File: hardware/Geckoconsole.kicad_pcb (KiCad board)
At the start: 2 copper layers, 68.6 x 41.9 mm, 51 parts, among them J21 I²C, J31 Conn_01x07_Female, J50 USB-C, J71 Conn_01x07, Q51 S8050, Q52 S8050, SW2 Reset, SW41 Rotary_Encoder_Switch, U1 ESP32-WROOM-32, U101 AMS1117-3.3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

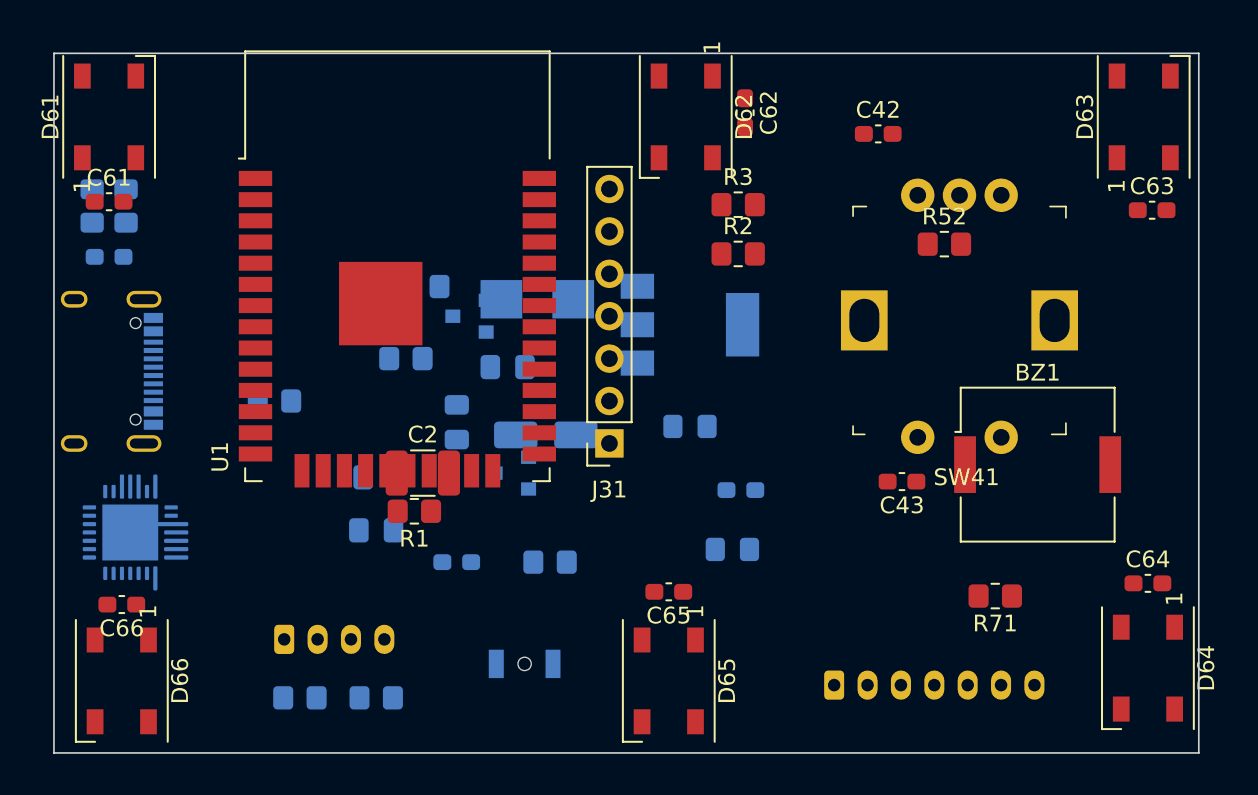
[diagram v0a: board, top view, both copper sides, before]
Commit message: Console Hardware: Place & Route PCB
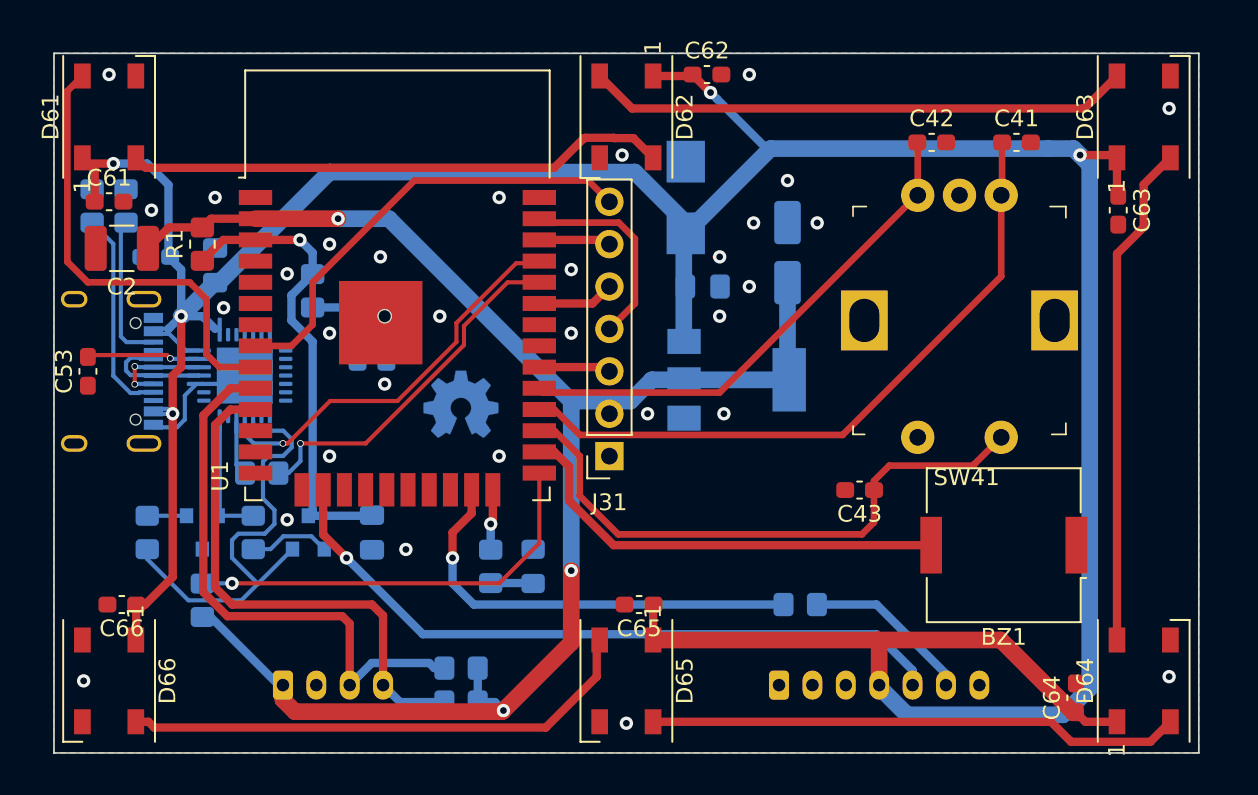
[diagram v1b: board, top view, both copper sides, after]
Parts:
- removed D102: LED, LED_SMD:LED_0805_2012Metric_Pad1.15x1.40mm_HandSolder
- removed R2: 470R, Resistor_SMD:R_0805_2012Metric_Pad1.20x1.40mm_HandSolder
- added LOGO1: Logo_Open_Hardware_Small, Fraxinas:OSHW-Logo_5.7x6mm_Mask, B.Cu at (75.2, 57.7)
- C41: moved to F.Cu
- C53: footprint Capacitor_SMD:C_0805_2012Metric_Pad1.18x1.45mm_HandSolder -> Capacitor_SMD:C_0603_1608Metric_Pad1.08x0.95mm_HandSolder; moved to F.Cu
- R3, R52, R71: moved to B.Cu
- moved R52 44.9 mm to (62.7, 64.3), turned to 90 degrees
- moved C41 26.6 mm to (108.5, 40.9)
- moved R3 26.3 mm to (77.0, 66.3), turned to 90 degrees
- moved R53 23.0 mm to (59.7, 68.3), turned to 90 degrees
- moved C2 22.5 mm to (54.9, 47.2), turned to 180 degrees
- moved SW2 22.5 mm to (70.6, 51.3)
- moved R55 21.6 mm to (66.3, 49.8), turned to 90 degrees
- moved Q51 20.6 mm to (59.7, 64.3), turned to 270 degrees
- moved R1 20.4 mm to (59.7, 47.0), turned to 90 degrees
- moved R51 18.7 mm to (56.4, 64.3), turned to 270 degrees
- moved C53 18.6 mm to (52.8, 54.6), turned to 90 degrees
- moved C102 18.1 mm to (94.7, 47.5), turned to 90 degrees
- moved C51 17.3 mm to (60.5, 48.3), turned to 90 degrees
- moved C55 13.0 mm to (69.8, 54.1), turned to 0 degrees
- moved Q52 12.7 mm to (66.0, 64.3), turned to 90 degrees
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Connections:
- BZ1 pad 1: Net-(BZ1-Pad1) -> GND
- BZ1 pad 2: GND -> Net-(BZ1-Pad2)
- J31 pad 4: SPI_MISO -> SPI_MOSI
- U1 pad 13: TX1 -> (no net)
- U1 pad 14: ENC_SW -> (no net)
- U1 pad 16: RGB -> TX1
- U1 pad 26: ENC_A -> Net-(BZ1-Pad2)
- U1 pad 27: SPI_BL -> ENC_SW
- U1 pad 28: SPI_DC -> ENC_A
- U1 pad 31: SPI_MISO -> (no net)
- U1 pad 36: (no net) -> SPI_DC
- U1 pad 37: (no net) -> SPI_MOSI
- U1 pad 8: Net-(BZ1-Pad1) -> SPI_BL
- U1 pad 9: (no net) -> RGB
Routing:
- net +5V: track 0.00 -> 210.8 mm, vias 0 -> 5
- net +3V3: track 0.00 -> 95.0 mm, vias 0 -> 3
- net TX1: track 0.00 -> 42.2 mm, vias 0 -> 1
- net ENC_A: track 0.00 -> 40.3 mm
- net ENC_SW: track 0.00 -> 35.7 mm
- net I2C_SDI: track 0.00 -> 34.0 mm
- net Net-(D62-Pad2): track 0.00 -> 32.6 mm
- net Net-(D61-Pad2): track 0.00 -> 32.5 mm
- net Net-(D64-Pad2): track 0.00 -> 32.0 mm
- net I2C_SCK: track 0.00 -> 31.6 mm
- net Net-(D65-Pad2): track 0.00 -> 31.3 mm
- net ENC_B: track 0.00 -> 30.9 mm
- net Net-(D63-Pad2): track 0.00 -> 30.2 mm
- net EN: track 0.00 -> 28.2 mm, vias 0 -> 1
- net IO0: track 0.00 -> 27.5 mm, vias 0 -> 1
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- added copper zone on B.Cu, net GND
- added copper zone on F.Cu, net GND

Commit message: Console Hardware: Add Extension header, PCB silkscreen labels
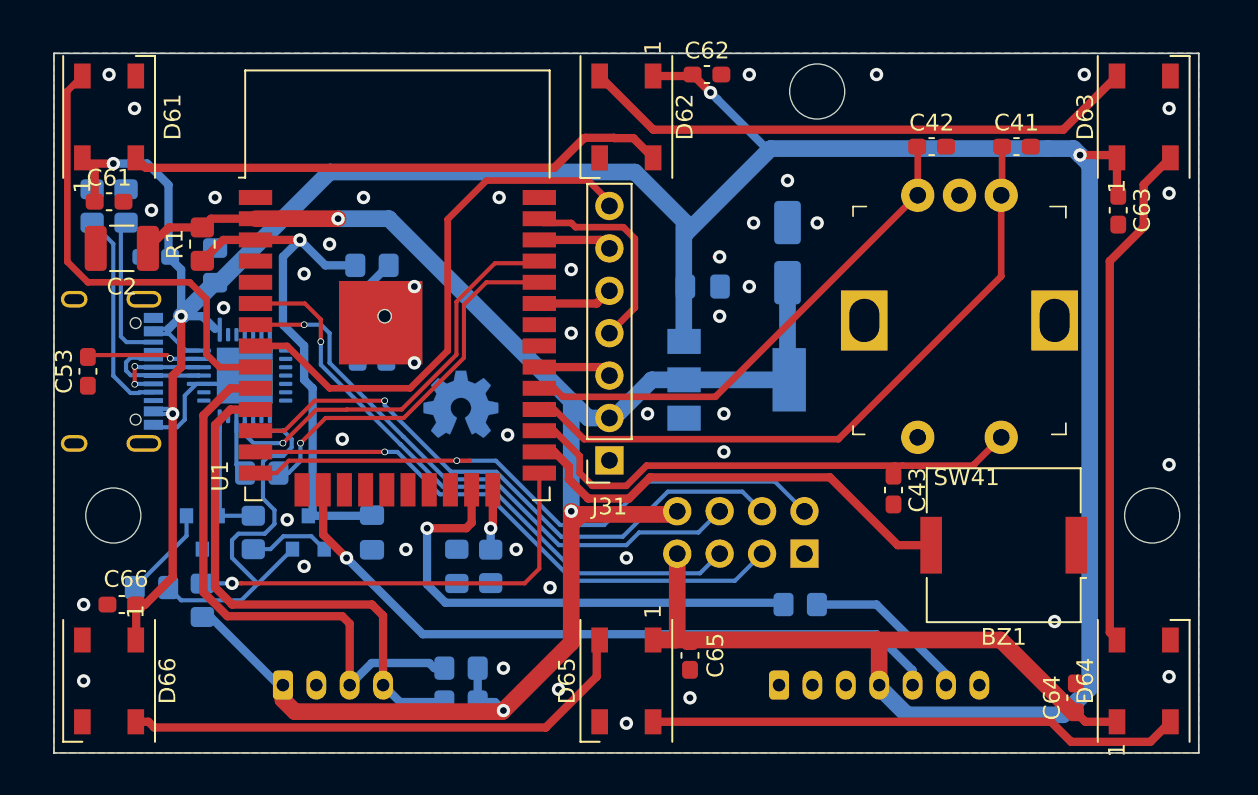
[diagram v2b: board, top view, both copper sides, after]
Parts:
- removed D101: B240, Diode_SMD:D_SMB
- added J1: Conn_01x08_Male, Connector_PinHeader_2.54mm:PinHeader_2x04_P2.54mm_Vertical, B.Cu at (95.8, 65.5)
- moved D1 4.57 mm to (74.9, 66.3)
- moved C65 4.31 mm to (88.9, 71.6), turned to 270 degrees
- moved R55 3.87 mm to (69.8, 48.3), turned to 180 degrees
- moved R51 3.31 mm to (56.6, 67.6), turned to 0 degrees
- moved C43 2.03 mm to (101.1, 61.7), turned to 270 degrees
- moved C41 0.25 mm to (108.5, 41.1)
- moved C42 0.25 mm to (103.4, 41.1)
- moved J31 0.25 mm to (84.1, 59.9)
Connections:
- U1 pad 12: (no net) -> GPIO27
- U1 pad 13: (no net) -> GPIO14
- U1 pad 14: (no net) -> GPIO12
- U1 pad 6: (no net) -> GPIO34
- U1 pad 7: (no net) -> GPIO35
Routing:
- net GPIO12: track 0.00 -> 37.4 mm, vias 0 -> 1
- net GPIO34: track 0.00 -> 36.6 mm, vias 0 -> 1
- net GPIO27: track 0.00 -> 36.2 mm, vias 0 -> 1
- net GPIO35: track 0.00 -> 35.2 mm, vias 0 -> 1
- net GPIO14: track 0.00 -> 34.2 mm, vias 0 -> 1
- net +3V3: track 95.0 -> 102.6 mm
- net SPI_BL: track 27.3 -> 32.5 mm
- net ENC_SW: track 35.7 -> 31.6 mm
- net EN: track 28.2 -> 32.1 mm
- net RX1: track 26.5 -> 30.0 mm
- net +5V: track 210.8 -> 214.1 mm
- net Net-(Q51-Pad1): track 2.35 -> 5.59 mm
- net /RTS: track 27.4 -> 24.9 mm
- net Net-(D1-Pad2): track 2.55 -> 0.00 mm
- net RXD0: track 21.7 -> 22.9 mm
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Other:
- outline, holes or cut-outs redrawn

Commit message: Console PCB: Drill holes
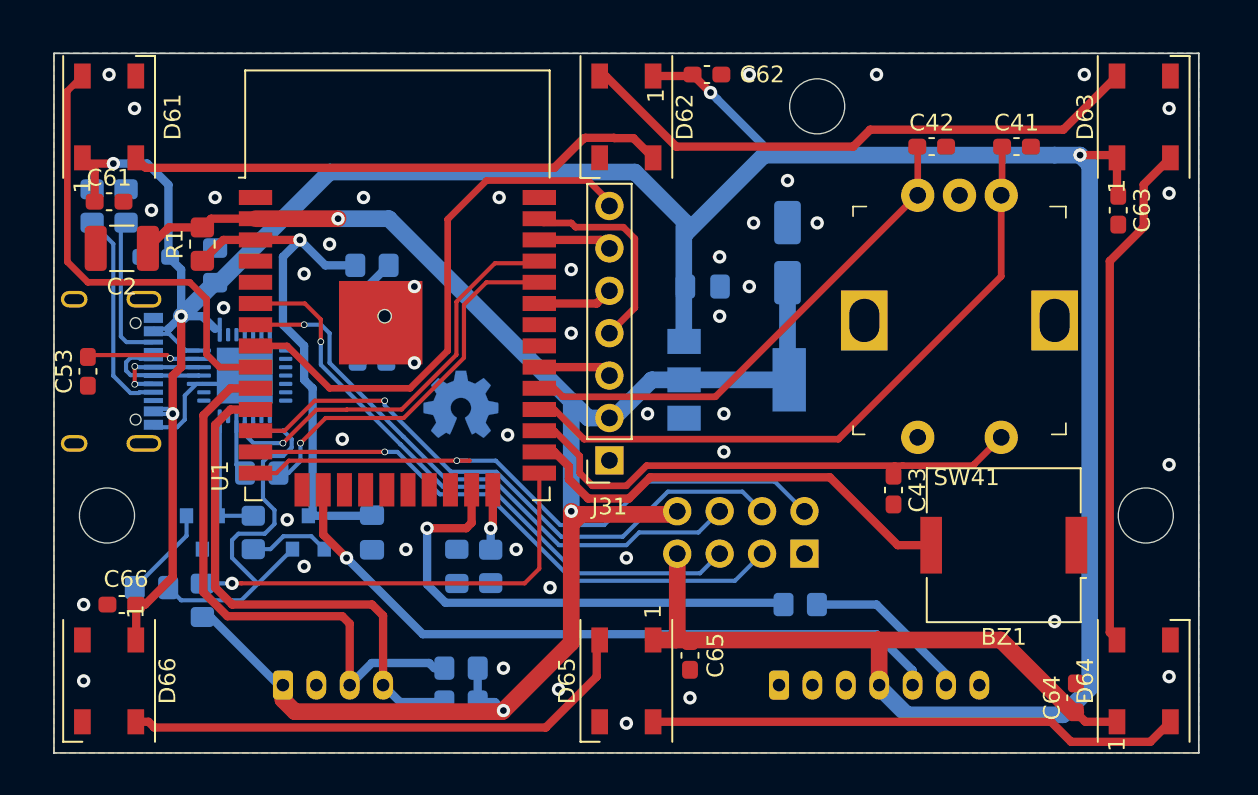
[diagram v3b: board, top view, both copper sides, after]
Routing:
- net Net-(D62-Pad2): track 33.6 -> 34.5 mm
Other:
- outline, holes or cut-outs redrawn
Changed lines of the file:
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@@
     (thickness 1.6)
     (drawings 10)
-    (tracks 484)
+    (tracks 486)
     (zones 0)
     (modules 50)
@@
     (42 Eco1.User user)
     (43 Eco2.User user)
-    (44 Edge.Cuts user hide)
+    (44 Edge.Cuts user)
     (45 Margin user)
     (46 B.CrtYd user)
@@
     (tags "capacitor handsolder")
     (attr smd)
-    (fp_text reference C62 (at 0 -1.43) (layer F.SilkS)
+    (fp_text reference C62 (at 3.302 0) (layer F.SilkS)
       (effects (font (size 1 1) (thickness 0.15)))
     )
@@
       (effects (font (size 0.8 0.8) (thickness 0.15)))
     )
-    (fp_text user 1 (at -4.15 -1.6 90) (layer F.SilkS)
+    (fp_text user 1 (at -3.81 -1.6 90) (layer F.SilkS)
       (effects (font (size 1 1) (thickness 0.15)))
     )
@@
       (effects (font (size 0.8 0.8) (thickness 0.15)))
     )
-    (fp_text user 1 (at -4.15 -1.6 90) (layer F.SilkS)
+    (fp_text user 1 (at -1.27 -1.778 90) (layer F.SilkS)
       (effects (font (size 1 1) (thickness 0.15)))
     )
@@
     )
   )
-  (gr_circle (center 96.52 37.846) (end 98.17 37.846) (layer Edge.Cuts) (width 0.05))
-  (gr_circle (center 116.586 63.246) (end 118.236 63.246) (layer Edge.Cuts) (width 0.05))
-  (gr_circle (center 54.356 63.246) (end 56.006 63.246) (layer Edge.Cuts) (width 0.05))
+  (gr_circle (center 96.52 38.734) (end 98.17 38.734) (layer Edge.Cuts) (width 0.05))
+  (gr_circle (center 116.206 63.246) (end 117.856 63.246) (layer Edge.Cuts) (width 0.05))
+  (gr_circle (center 53.976 63.246) (end 55.626 63.246) (layer Edge.Cuts) (width 0.05))
   (gr_circle (center 54.356 63.246) (end 53.086 61.722) (layer Dwgs.User) (width 0.15))
   (gr_circle (center 54.102 62.992) (end 53.848 63.246) (layer Dwgs.User) (width 0.15))
@@
   (segment (start 114.478 41.82) (end 114.478 43.7125) (width 0.5) (layer F.Cu) (net 4))
   (segment (start 60.4305 49.2975) (end 58.42 51.308) (width 1) (layer B.Cu) (net 4))
-  (segment (start 88.646 45.72) (end 88.646 46.346) (width 1) (layer B.Cu) (net 4))
-  (segment (start 67.31 42.672) (end 85.598 42.672) (width 1) (layer B.Cu) (net 4))
-  (segment (start 85.598 42.672) (end 88.646 45.72) (width 1) (layer B.Cu) (net 4))
-  (segment (start 60.6845 49.2975) (end 67.31 42.672) (width 1) (layer B.Cu) (net 4))
-  (segment (start 88.646 46.346) (end 93.726 41.266) (width 1) (layer B.Cu) (net 4))
-  (segment (start 93.726 41.266) (end 110.354 41.266) (width 1) (layer B.Cu) (net 4))
-  (segment (start 110.354 41.266) (end 111.878 41.266) (width 1) (layer B.Cu) (net 4))
-  (segment (start 111.878 41.266) (end 112.268 41.656) (width 1) (layer B.Cu) (net 4))
   (via (at 112.268 41.656) (size 0.8) (drill 0.4) (layers F.Cu B.Cu) (net 4))
   (segment (start 114.314 41.656) (end 114.478 41.82) (width 0.5) (layer F.Cu) (net 4))
@@
   (segment (start 89.0535 36.83) (end 90.131504 37.908004) (width 0.5) (layer F.Cu) (net 4))
   (segment (start 90.131504 37.908004) (end 90.131504 37.908014) (width 0.5) (layer F.Cu) (net 4))
-  (segment (start 93.726 41.266) (end 93.48949 41.266) (width 0.5) (layer B.Cu) (net 4))
-  (segment (start 93.48949 41.266) (end 90.531503 38.308013) (width 0.5) (layer B.Cu) (net 4))
-  (segment (start 90.531503 38.308013) (end 90.131504 37.908014) (width 0.5) (layer B.Cu) (net 4))
   (segment (start 53.2395 42.5575) (end 52.502 41.82) (width 0.5) (layer F.Cu) (net 4))
   (segment (start 53.2395 44.45) (end 53.2395 42.5575) (width 0.5) (layer F.Cu) (net 4))
@@
   (segment (start 88.048 70.702) (end 86.840002 70.702) (width 1) (layer F.Cu) (net 4))
   (segment (start 100.166 70.702) (end 88.048 70.702) (width 1) (layer F.Cu) (net 4))
+  (segment (start 90.531503 38.308013) (end 90.131504 37.908014) (width 0.5) (layer B.Cu) (net 4))
+  (segment (start 93.87949 41.656) (end 90.531503 38.308013) (width 0.5) (layer B.Cu) (net 4))
+  (segment (start 93.98 41.656) (end 93.87949 41.656) (width 0.5) (layer B.Cu) (net 4))
+  (segment (start 88.646 46.346) (end 93.336 41.656) (width 1) (layer B.Cu) (net 4))
+  (segment (start 88.646 45.72) (end 88.646 46.346) (width 1) (layer B.Cu) (net 4))
+  (segment (start 110.744 41.656) (end 112.268 41.656) (width 1) (layer B.Cu) (net 4))
+  (segment (start 85.598 42.672) (end 88.646 45.72) (width 1) (layer B.Cu) (net 4))
+  (segment (start 93.336 41.656) (end 110.744 41.656) (width 1) (layer B.Cu) (net 4))
+  (segment (start 67.31 42.672) (end 85.598 42.672) (width 1) (layer B.Cu) (net 4))
+  (segment (start 60.6845 49.2975) (end 67.31 42.672) (width 1) (layer B.Cu) (net 4))
   (segment (start 59.48 53.864) (end 57.928 53.864) (width 0.25) (layer B.Cu) (net 5))
   (via (at 57.77 53.835) (size 0.4) (drill 0.3) (layers F.Cu B.Cu) (net 5))
@@
   (segment (start 59.944 50.292) (end 58.928 49.276) (width 0.4) (layer F.Cu) (net 9))
   (segment (start 62.874 54.356) (end 60.706 54.356) (width 0.4) (layer F.Cu) (net 9))
-  (segment (start 86.702 40.132) (end 83.49 36.92) (width 0.5) (layer F.Cu) (net 10))
-  (segment (start 111.266 40.132) (end 86.702 40.132) (width 0.5) (layer F.Cu) (net 10))
+  (segment (start 83.850002 36.92) (end 83.49 36.92) (width 0.5) (layer F.Cu) (net 10))
+  (segment (start 88.078002 41.148) (end 83.850002 36.92) (width 0.5) (layer F.Cu) (net 10))
+  (segment (start 99.695 40.132) (end 98.679 41.148) (width 0.5) (layer F.Cu) (net 10))
+  (segment (start 98.679 41.148) (end 88.078002 41.148) (width 0.5) (layer F.Cu) (net 10))
+  (segment (start 111.266 40.132) (end 99.695 40.132) (width 0.5) (layer F.Cu) (net 10))
   (segment (start 114.478 36.92) (end 111.266 40.132) (width 0.5) (layer F.Cu) (net 10))
   (segment (start 114.478 70.702) (end 114.48199 70.69801) (width 0.5) (layer F.Cu) (net 11))

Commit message: Console Schema+PCB: Add pull-up resistors for rotary encoder
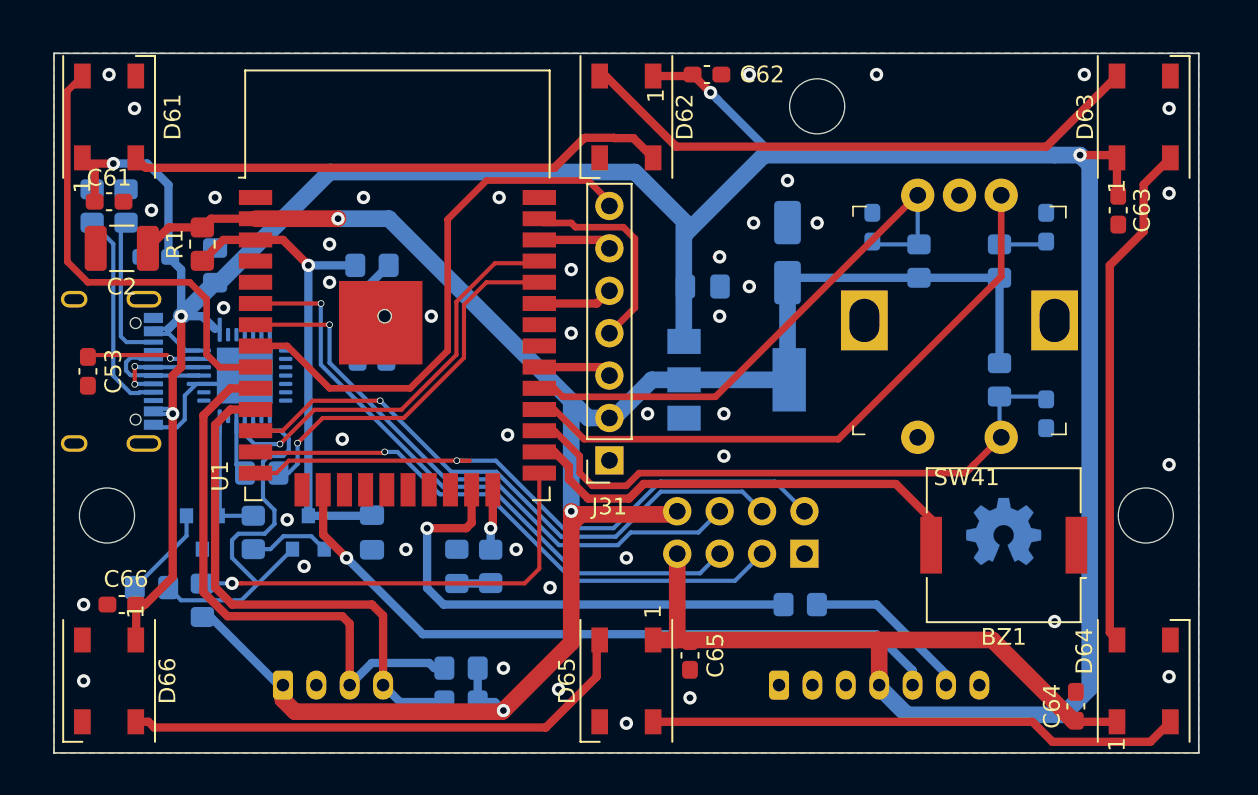
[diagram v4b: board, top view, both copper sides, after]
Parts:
- added R41: 68k, Resistor_SMD:R_0805_2012Metric_Pad1.20x1.40mm_HandSolder, B.Cu at (107.4, 48.0)
- added R42: 68k, Resistor_SMD:R_0805_2012Metric_Pad1.20x1.40mm_HandSolder, B.Cu at (102.6, 48.0)
- added R43: 68k, Resistor_SMD:R_0805_2012Metric_Pad1.20x1.40mm_HandSolder, B.Cu at (107.4, 55.1)
- C41, C42, C43: moved to B.Cu
- moved LOGO1 33.4 mm to (107.7, 65.3)
- moved C43 10.2 mm to (110.2, 57.1)
- moved C42 5.99 mm to (99.8, 46.0), turned to 90 degrees
- moved C41 5.14 mm to (110.2, 46.0), turned to 90 degrees
- moved C64 0.51 mm to (112.0, 74.7)
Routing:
- net +3V3: track 102.6 -> 120.6 mm
- net ENC_SW: track 31.6 -> 36.4 mm
- net EN: track 32.1 -> 29.1 mm
- net ENC_A: track 40.5 -> 43.2 mm
- net ENC_B: track 31.1 -> 33.7 mm
- net Net-(D1-Pad2): track 0.00 -> 2.04 mm
- net Net-(BZ1-Pad2): track 27.3 -> 27.9 mm
- net GPIO34: track 36.6 -> 37.2 mm
- net GND: vias 40 -> 41
- net (no net): vias 4 -> 2
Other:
- board text added: "Reset"
